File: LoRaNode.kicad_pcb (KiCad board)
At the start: 2 copper layers, 45 x 53 mm, 32 parts, among them J1 Conn_01x09, J2 Conn_01x03, J4 ISP, J5 Conn_01x06, J8 D2, J9 D3, SW1 SW_Push, U1 RFM95W-868S2, U4 ATMEGA328P-AU, Y1 8MHz HC5032/4

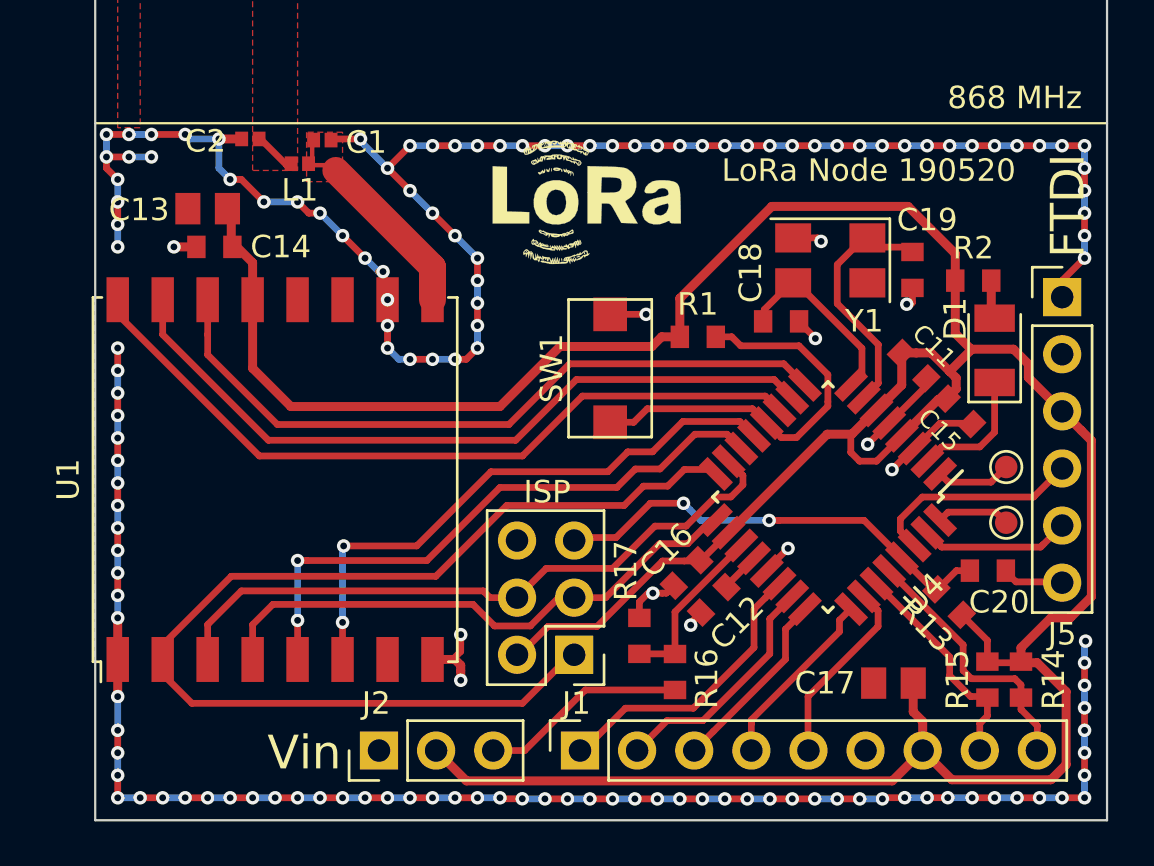
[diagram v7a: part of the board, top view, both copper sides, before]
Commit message: Added mounting holes
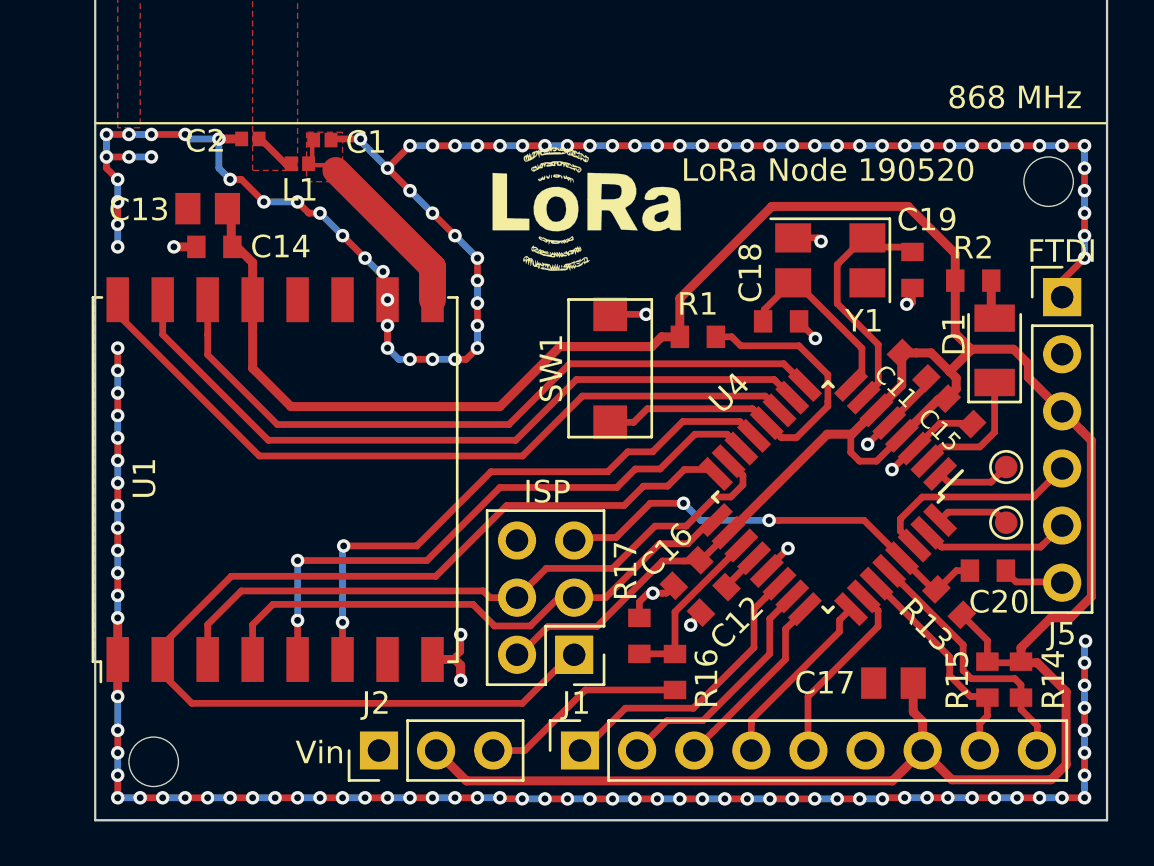
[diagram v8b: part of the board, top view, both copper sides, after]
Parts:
- added J3: Conn_01x01, MountingHole:MountingHole_2.2mm_M2, F.Cu at (169.4, 90.6)
- added J6: Conn_01x01, MountingHole:MountingHole_2.2mm_M2, F.Cu at (129.6, 116.4)
- U1: footprint riske:HOPERF_RFM95W_SMD -> MYLIB:HOPERF_RFM95W_SMD
- moved G*** 0.30 mm to (149.3, 92.2)
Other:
- board text added: "GND max 3.9V VCC B"
- board text removed: "G + B"
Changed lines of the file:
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@@
     (tracks 652)
     (zones 0)
-    (modules 32)
+    (modules 34)
     (nets 33)
   )
@@
   )
   (layers
-    (0 F.Cu signal)
+    (0 F.Cu signal hide)
     (31 B.Cu signal)
     (32 B.Adhes user)
@@
     (solder_mask_min_width 0.25)
     (aux_axis_origin 150 50)
-    (visible_elements 7FFFEFFF)
+    (visible_elements 7FFFFFFF)
     (pcbplotparams
       (layerselection 0x010f0_ffffffff)
@@
   )
   (module kicad-footprints-master:LoRa-Logo-Small (layer F.Cu)
-    (at 149.3 91.9)
+    (at 149.3 92.2)
     (fp_text reference G*** (at 0 0) (layer F.SilkS) hide
       (effects (font (size 1.524 1.524) (thickness 0.3)))
@@
     (tags diode)
     (attr smd)
-    (fp_text reference D1 (at 1.4 -1.75 90) (layer F.SilkS)
+    (fp_text reference D1 (at 0.7 -1.8 90) (layer F.SilkS)
       (effects (font (size 1 1) (thickness 0.15)))
     )
@@
     (tags capacitor)
     (attr smd)
-    (fp_text reference C11 (at 0.012728 -1.260064 315) (layer F.SilkS)
+    (fp_text reference C11 (at 0.083439 1.214809 315) (layer F.SilkS)
       (effects (font (size 0.8 0.8) (thickness 0.15)))
     )
@@
     (tags "QFP 0.8")
     (attr smd)
-    (fp_text reference U4 (at 0 -6.05 225) (layer F.SilkS)
+    (fp_text reference U4 (at -0.165463 6.373861 225) (layer F.SilkS)
       (effects (font (size 1 1) (thickness 0.15)))
     )
@@
     )
   )
-  (module riske:HOPERF_RFM95W_SMD (layer F.Cu)
+  (module MYLIB:HOPERF_RFM95W_SMD (layer F.Cu)
     (at 135 103.85 90)
     (descr "Low Power Long Range Transceiver Module SMD-16 (https://www.hoperf.com/data/upload/portal/20181127/5bfcbea20e9ef.pdf)")
     (tags "LoRa Low Power Long Range Transceiver Module")
     (attr smd)
-    (fp_text reference U1 (at 0 -9.2 90) (layer F.SilkS)
+    (fp_text reference U1 (at 0.05 -5.8 90) (layer F.SilkS)
       (effects (font (size 1 1) (thickness 0.15)))
     )
@@
       (rotate (xyz 0 0 0))
     )
-    (model "E:/download/RFM95 LoRa v15.step"
+    (model ${MYLIB}/HOPERF_RFM95W_SMD.step
       (offset (xyz -8 8 0))
       (scale (xyz 1 1 1))
       (rotate (xyz -90 0 0))
     )
+  )
+  (module MountingHole:MountingHole_2.2mm_M2 (layer F.Cu)
+    (at 169.4 90.6)
+    (descr "Mounting Hole 2.2mm, no annular, M2")
+    (tags "mounting hole 2.2mm no annular m2")
+    (attr virtual)
+    (fp_text reference J3 (at 0 -3.2) (layer F.SilkS) hide
+      (effects (font (size 1 1) (thickness 0.15)))
+    )
+    (fp_text value Conn_01x01 (at 0 3.2) (layer F.Fab)
+      (effects (font (size 1 1) (thickness 0.15)))
+    )
+    (fp_circle (center 0 0) (end 2.45 0) (layer F.CrtYd) (width 0.05))
+    (fp_circle (center 0 0) (end 2.2 0) (layer Cmts.User) (width 0.15))
+    (fp_text user %R (at 0.3 0) (layer F.Fab)
+      (effects (font (size 1 1) (thickness 0.15)))
+    )
+    (pad 1 np_thru_hole circle (at 0 0) (size 2.2 2.2) (drill 2.2) (layers *.Cu *.Mask))
+  )
+  (module MountingHole:MountingHole_2.2mm_M2 (layer F.Cu)
+    (at 129.6 116.4)
+    (descr "Mounting Hole 2.2mm, no annular, M2")
+    (tags "mounting hole 2.2mm no annular m2")
+    (attr virtual)
+    (fp_text reference J6 (at 0 -3.2) (layer F.SilkS) hide
+      (effects (font (size 1 1) (thickness 0.15)))
+    )
+    (fp_text value Conn_01x01 (at 0 3.2) (layer F.Fab)
+      (effects (font (size 1 1) (thickness 0.15)))
+    )
+    (fp_text user %R (at 0.3 0) (layer F.Fab)
+      (effects (font (size 1 1) (thickness 0.15)))
+    )
+    (fp_circle (center 0 0) (end 2.2 0) (layer Cmts.User) (width 0.15))
+    (fp_circle (center 0 0) (end 2.45 0) (layer F.CrtYd) (width 0.05))
+    (pad 1 np_thru_hole circle (at 0 0) (size 2.2 2.2) (drill 2.2) (layers *.Cu *.Mask))
   )
   (gr_text "SCL\nSDA\n3V3\nGND\nA3\nA2\nA1\nA0\nA7" (at 158.7 114.8 270) (layer B.SilkS)
     (effects (font (size 1.5 1.5) (thickness 0.3)) (justify left mirror))
   )
-  (gr_text Vin (at 136.3 116) (layer F.SilkS)
-    (effects (font (size 1.5 1.5) (thickness 0.3)))
-  )
-  (gr_text "LoRa Node 190520" (at 159.512 90.678) (layer B.SilkS)
+  (gr_text Vin (at 137 116) (layer F.SilkS)
+    (effects (font (size 1 1) (thickness 0.15)))
+  )
+  (gr_text "LoRa Node 190520" (at 156.2 90.3) (layer B.SilkS)
     (effects (font (size 1.5 1.5) (thickness 0.3)) (justify mirror))
   )
-  (gr_text "LoRa Node 190520" (at 161.4 90.1) (layer F.SilkS)
+  (gr_text "LoRa Node 190520" (at 159.6 90.1) (layer F.SilkS)
     (effects (font (size 1 1) (thickness 0.2)))
   )
@@
     (effects (font (size 1 1) (thickness 0.2)))
   )
-  (gr_text "G\n+\nB" (at 142 114.5 90) (layer B.SilkS)
+  (gr_text "GND\nmax 3.9V VCC\nB" (at 142 114.5 90) (layer B.SilkS)
     (effects (font (size 1.5 1.5) (thickness 0.3)) (justify right mirror))
   )
@@
   (gr_line (start 172 119) (end 172 66) (layer Edge.Cuts) (width 0.1))
   (gr_line (start 127 119) (end 172 119) (layer Edge.Cuts) (width 0.1))
-  (gr_text FTDI (at 170.258 91.67 90) (layer F.SilkS)
-    (effects (font (size 1.5 1.5) (thickness 0.3)))
+  (gr_text FTDI (at 170 93.7) (layer F.SilkS)
+    (effects (font (size 1 1) (thickness 0.15)))
   )
   (segment (start 134 110.3) (end 134.9 109.4) (width 0.3) (layer F.Cu) (net 1))
